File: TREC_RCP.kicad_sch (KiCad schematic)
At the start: 5 parts, among them J1 Raspberry_Pi_4

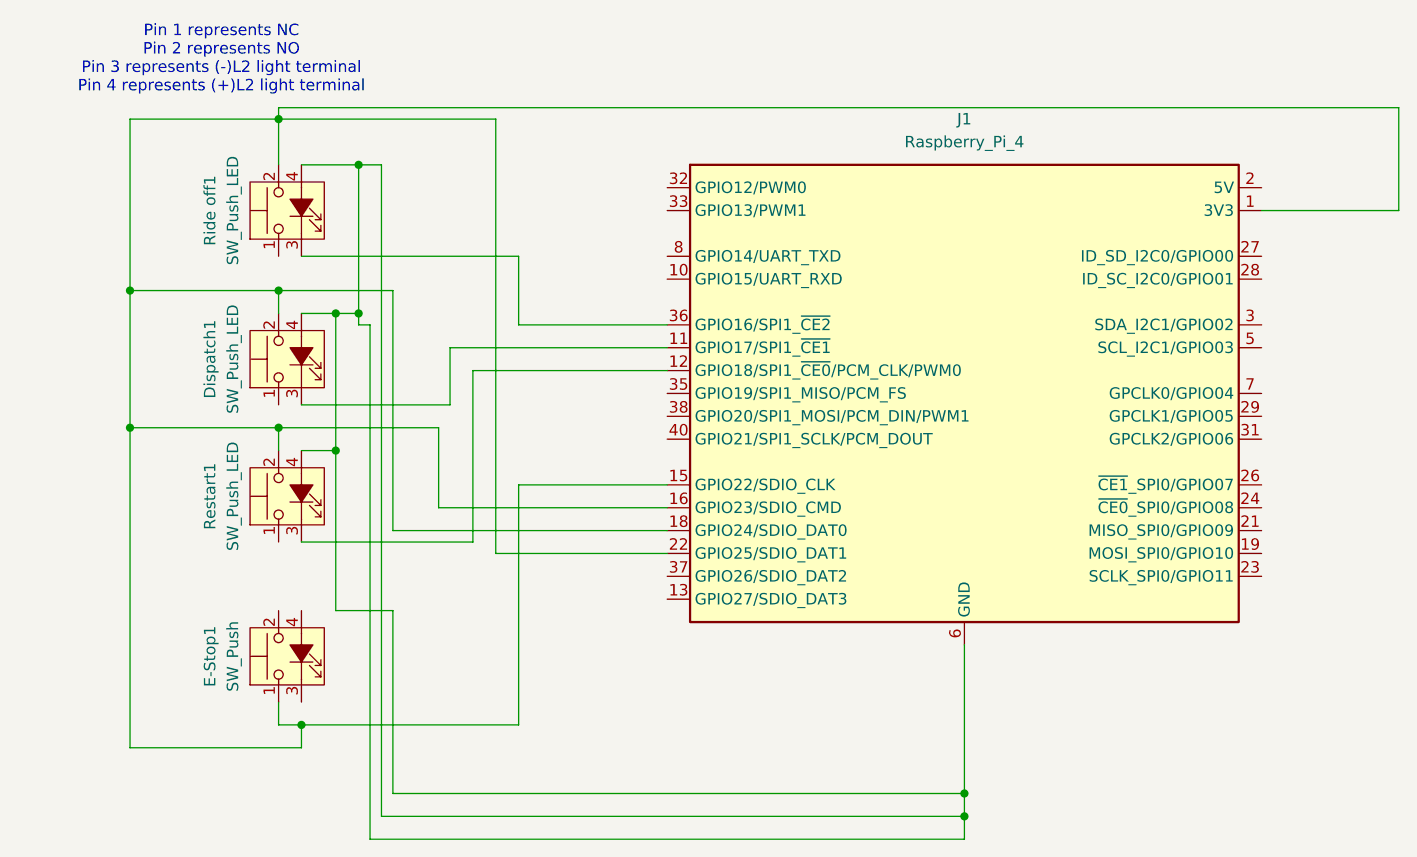
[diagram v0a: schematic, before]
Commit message: Update TREC_RCP.kicad_sch
Changed the coloring of wires to add a more clear distinction between lines and added the second dispatch button
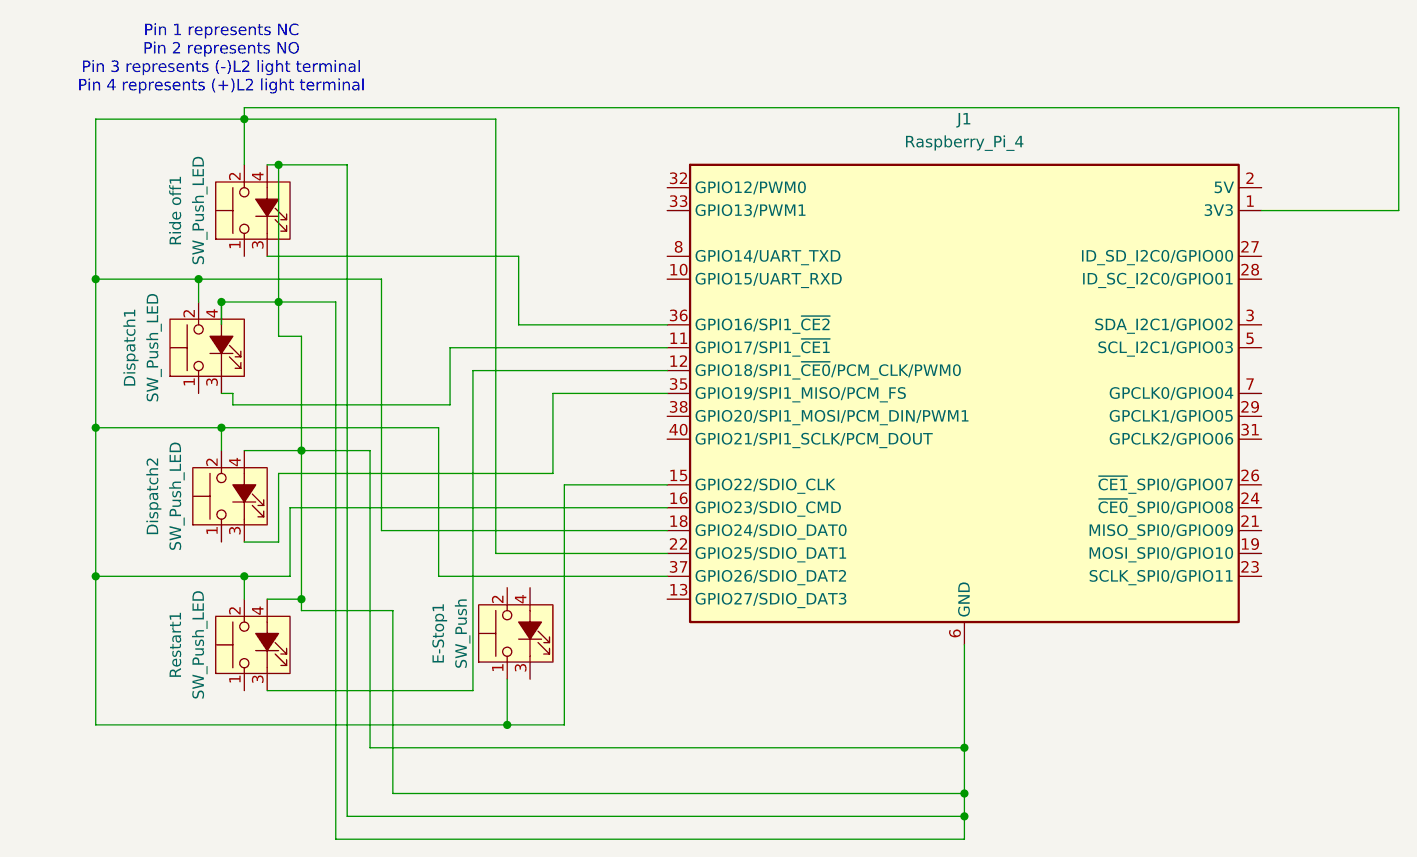
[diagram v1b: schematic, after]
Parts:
- added Dispatch2: SW_Push_LED, symbol Switch:SW_Push_LED
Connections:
- net at Dispatch1.2, E-Stop1.1, J1.1 (3V3)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: now also J1.37 (GPIO26/SDIO_DAT2), Dispatch2.2
- net at Dispatch1.4 (A), J1.14 (GND), J1.20 (GND)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: now also Dispatch2.4 (A)
- net at J1.35 (GPIO19/SPI1_MISO/PCM_FS): now also Dispatch2.3 (K)
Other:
- moved on the sheet: Dispatch1, E-Stop1, Restart1, Ride off1
